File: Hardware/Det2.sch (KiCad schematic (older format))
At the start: 48 parts, among them U3 MAX4477, U4 MAX4477, U5 MAX4477

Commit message: Clear annotations
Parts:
- renumbered C22 to C?, C28 to C?, C30 to C?, C26 to C?, C27 to C?, C29 to C?, C31 to C?, C32 to C?, C23 to C?, C24 to C?, C35 to C?, C33 to C?, C34 to C?, C25 to C?, C7 to C?, C46 to C?, D34 to D?, D32 to D?, D30 to D?, D28 to D?, D26 to D?, D24 to D?, D22 to D?, D20 to D?, D35 to D?, D33 to D?, D31 to D?, D29 to D?, D27 to D?, D25 to D?, D23 to D?, D21 to D?, R22 to R?, R24 to R?, R28 to R?, R29 to R?, R30 to R?, R25 to R?, R31 to R?, R32 to R?, R26 to R?, R27 to R?, R23 to R?, R40 to R?, R20 to R?, U3 to U?, U4 to U?, U5 to U?

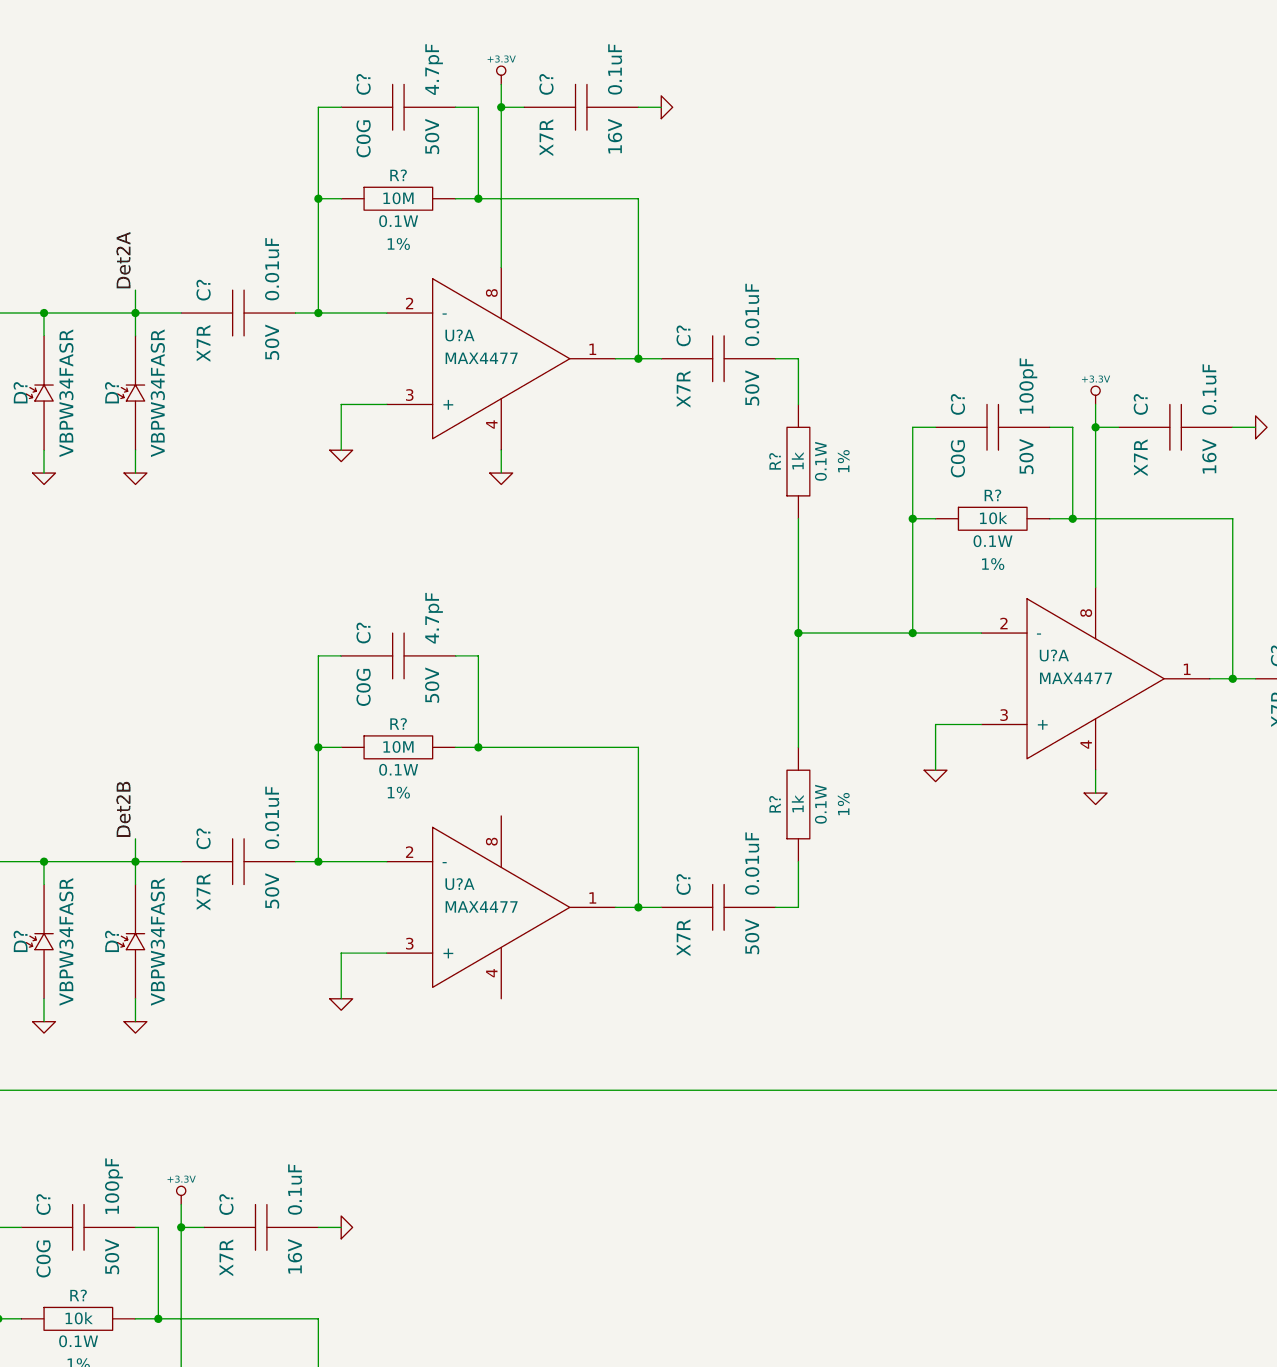
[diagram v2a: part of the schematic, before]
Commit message: Add LDO for analog
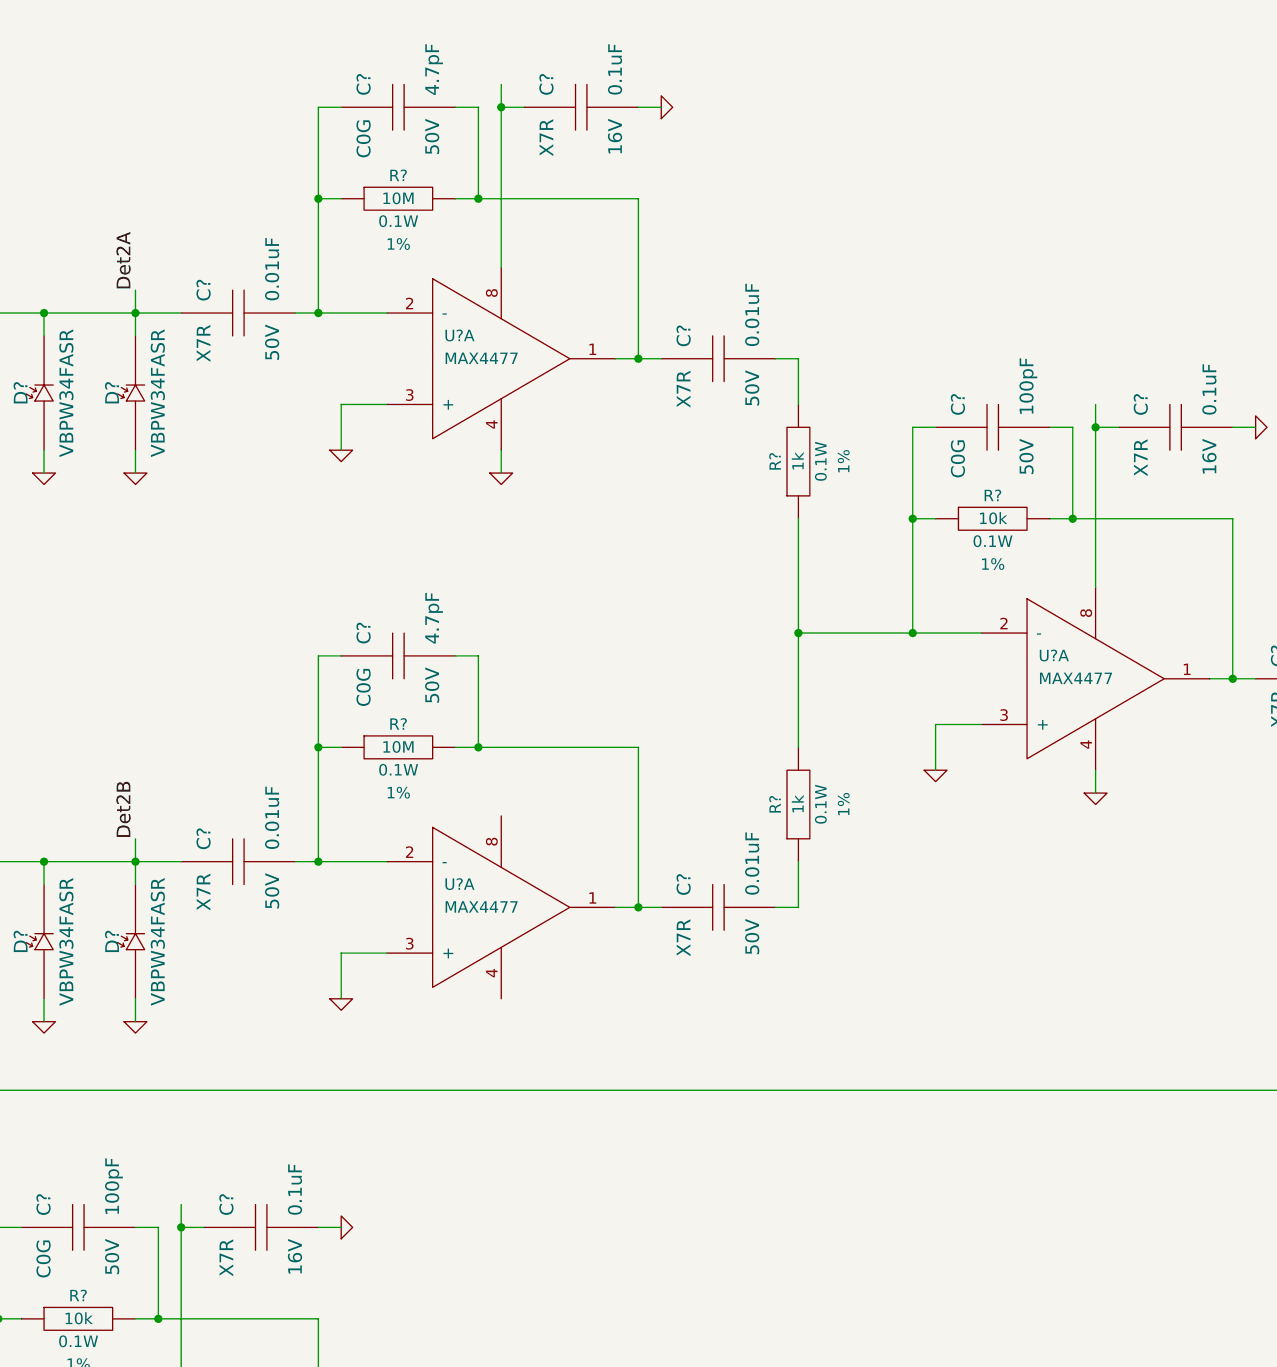
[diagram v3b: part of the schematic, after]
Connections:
- net labels removed: +3.3V
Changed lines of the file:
@@
 Sheet 4 5
 Title "Solid State Cosmic Ray Detector"
-Date "22 sep 2014"
+Date "23 sep 2014"
 Rev "1"
 Comp "Ethan Harstad"
@@
 $EndComp
 $Comp
-L +3.3V #PWR?
-U 1 1 52B9581C
-P 6200 900
-F 0 "#PWR?" H 6200 860 30  0001 C CNN
-F 1 "+3.3V" H 6200 1010 30  0000 C CNN
-F 2 "" H 6200 900 60  0000 C CNN
-F 3 "" H 6200 900 60  0000 C CNN
-	1    6200 900
-	1    0    0    -1
-$EndComp
-$Comp
 L C C?
 U 1 1 52B95827
@@
 	0    -1   -1   0
 $EndComp
-$Comp
-L +3.3V #PWR?
-U 1 1 52B95997
-P 8800 2300
-F 0 "#PWR?" H 8800 2260 30  0001 C CNN
-F 1 "+3.3V" H 8800 2410 30  0000 C CNN
-F 2 "" H 8800 2300 60  0000 C CNN
-F 3 "" H 8800 2300 60  0000 C CNN
-	1    8800 2300
-	1    0    0    -1
-$EndComp
 Wire Wire Line
 	7400 4500 7500 4500
@@
 $EndComp
 $Comp
-L +3.3V #PWR?
-U 1 1 52BB5C92
-P 4800 5800
-F 0 "#PWR?" H 4800 5760 30  0001 C CNN
-F 1 "+3.3V" H 4800 5910 30  0000 C CNN
-F 2 "" H 4800 5800 60  0000 C CNN
-F 3 "" H 4800 5800 60  0000 C CNN
-	1    4800 5800
-	1    0    0    -1
-$EndComp
-$Comp

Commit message: New detector chain
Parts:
- removed C? (x5): 0.1uF, CAPC1608, symbol C
- removed C? (x2): 4.7pF, CAPC1608, symbol C
- removed C? (x6): 0.01uF, CAPC1608, symbol C
- removed C? (x3): 100pF, CAPC1608, symbol C
- removed D? (x16): VBPW34FASR, DIOC-BPW34R, symbol DIODE-PHOTO
- removed R? (x2): 1M, RESC1608, symbol R
- removed R? (x4): 10M, RESC1608, symbol R
- removed R? (x4): 1k, RESC1608, symbol R
- removed R? (x3): 10k, RESC1608, symbol R
- removed U? (x5): MAX4477, symbol OPAMP-DUAL
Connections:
- net labels removed: +12V, Det2A, Det2B, GND, Out
- wire segments 120 -> 0

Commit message: Add second detector chain
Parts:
- added C? (x5): 0.1uF, CAPC1608, symbol C
- added C? (x5): 1000pF, CAPC1608, symbol C
- added C? (x2): C, ~, symbol C
- added D? (x16): VBPW34FASR, DIOC-BPW34R, symbol DIODE-PHOTO
- added R? (x4): 1M, RESC1608, symbol R
- added R? (x2): 10M, RESC1608, symbol R
- added R? (x3): 100k, ~, symbol R
- added R? (x4): 10k, RESC1608, symbol R
- added U? (x5): AD8616, ~, symbol OPAMP-DUAL
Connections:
- new net: C?.1, R?.1, R?.1 (x2)
- new net: C?.1, C?.2, R?.1, U?.2 (-) (x2)
- new net: C?.1, C?.2, R?.2, U?.1 (x2)
- new net: R?.1, R?.1, R?.2, U?.2 (-)
- new net: R?.2, R?.2, U?.1
- new net: C?.2, R?.2
- new net: C?.2, R?.1
- new net: C?.1, R?.1, R?.1, U?.2 (-)
- new net: C?.2, R?.2, R?.2, U?.1
- new net: R?.1, R?.1, U?.2 (-)
- new net Det1A: C?.1, D?.2, D?.2, D?.2, D?.2, D?.2, D?.2, D?.2, D?.2, R?.2
- new net Det1B: C?.1, D?.2, D?.2, D?.2, D?.2, D?.2, D?.2, D?.2, D?.2, R?.2
- new net GND: C?.2, C?.2, C?.2, C?.2, C?.2, D?.1, D?.1, D?.1, D?.1, D?.1, D?.1, D?.1, D?.1, D?.1, D?.1, D?.1, D?.1, D?.1, D?.1, D?.1, D?.1, U?.4, U?.4, U?.4
- new net Out: R?.2, U?.1
- new net Ref: U?.3 (+), U?.3 (+), U?.3 (+), U?.3 (+), U?.3 (+)
- new net VAA: C?.1, C?.1, C?.1, U?.8, U?.8, U?.8
- new net VCOM: R?.2, R?.2
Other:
- note added: "Charge Amplifier"
- note added: "Differentiator Amplifier"
- note added: "Final Amplifier"
- note added: "Integrator Amplifier"
- note added: "Light Shielding"
- note added: "Summing"

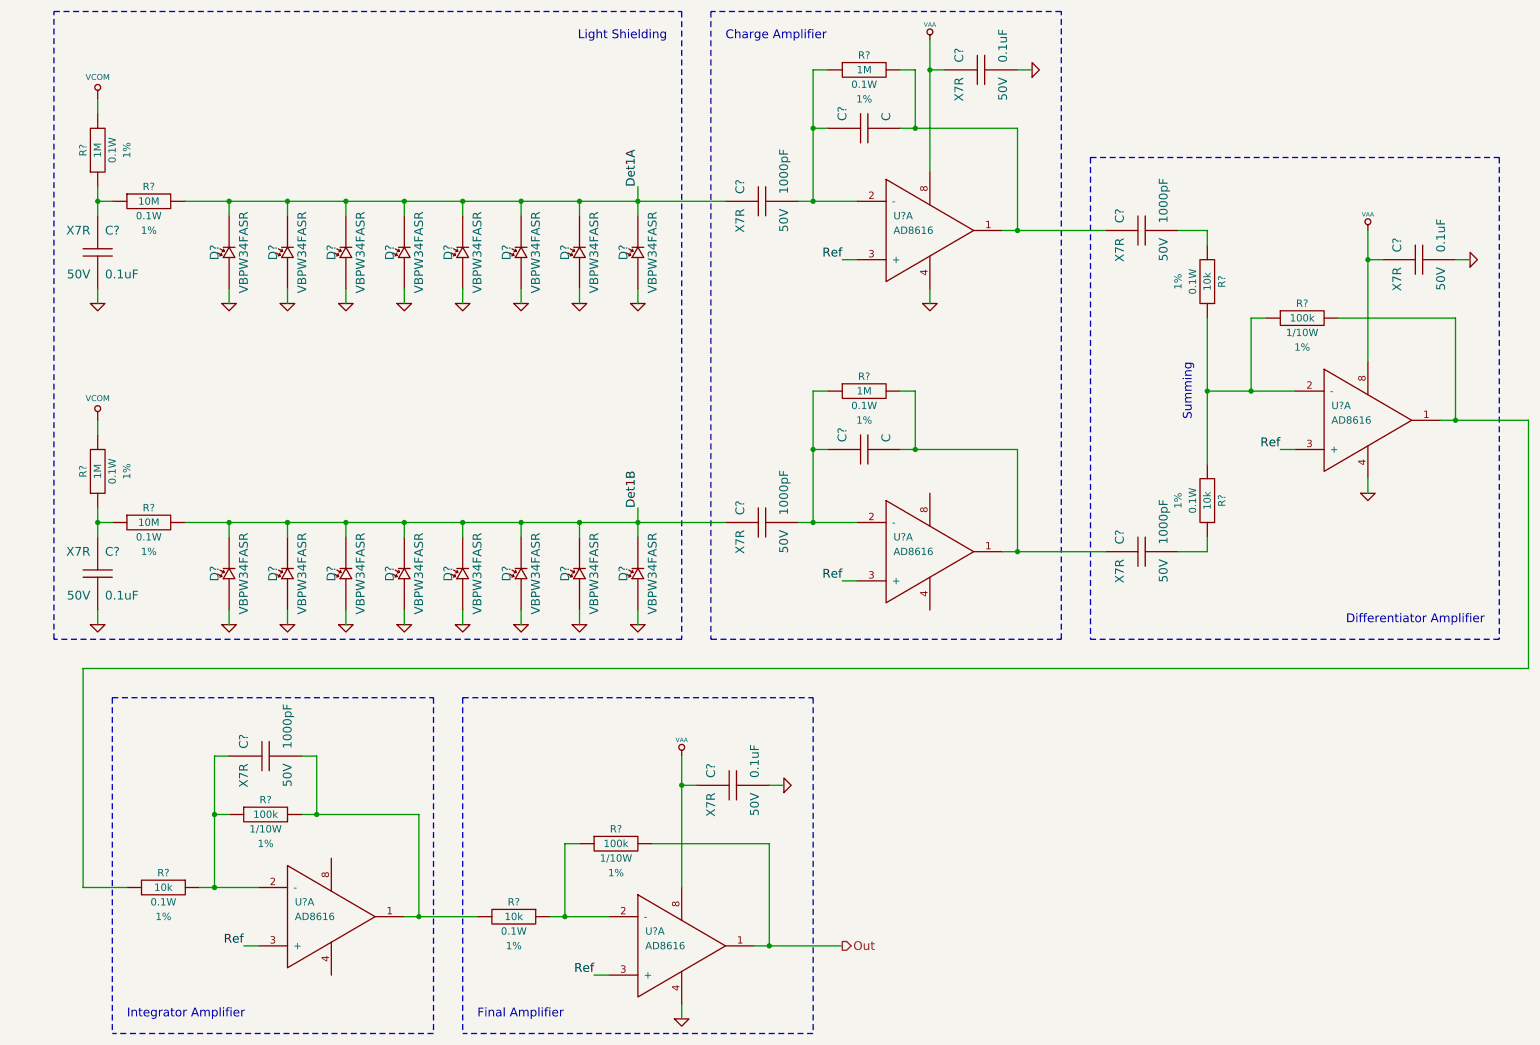
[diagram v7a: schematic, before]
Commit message: Rough layout for pin map testing
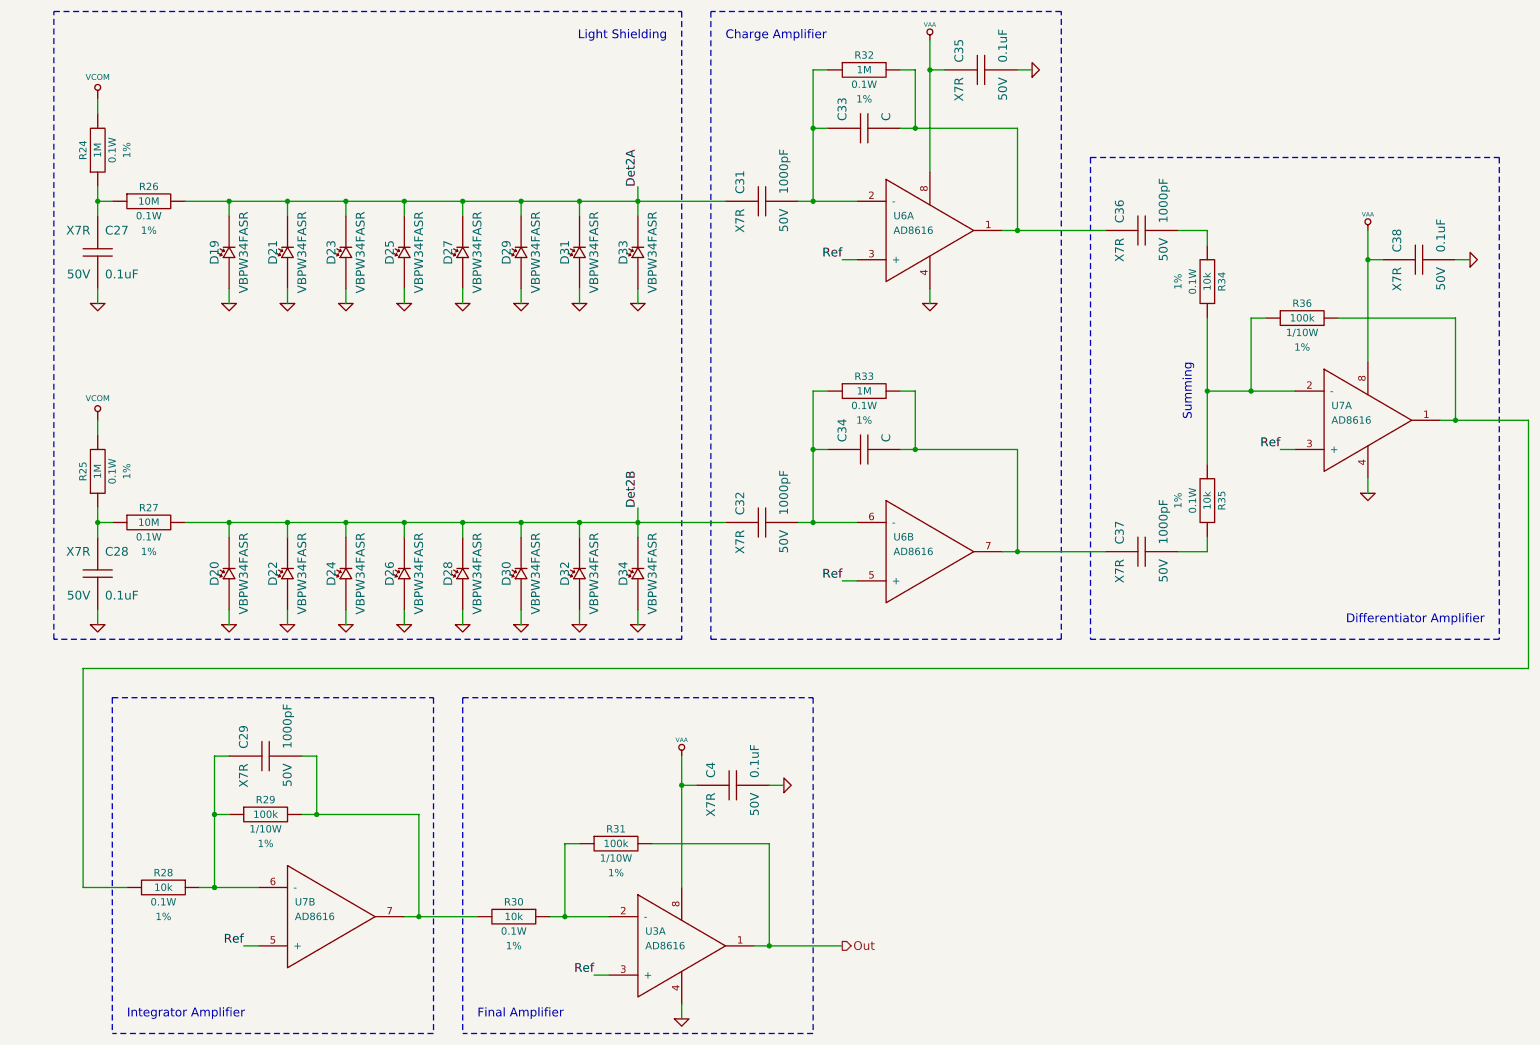
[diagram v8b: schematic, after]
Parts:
- removed C?: 0.1uF, CAPC1608, symbol C
- added C4: 0.1uF, CAPC1608, symbol C
- gave numbers to parts that had none: 43
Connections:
- net GND: now also U3.4, U7.4, C4.2; no longer U6.4, U7.4
- net Out: now also U3.1; no longer U6.1
- net Ref: now also U6.5 (+), U7.5 (+); no longer U6.3 (+), U7.3 (+)
- net VAA: now also U3.8, U7.8, C4.1; no longer U6.8, U7.8
- net at C31.2, C33.1, R32.1: now also U6.2 (-); no longer U6.2 (-)
- net at C33.2, C36.1, R32.2: now also U6.1; no longer U6.1
- net at C32.2, C34.1, R33.1: now also U6.6 (-); no longer U7.2 (-)
- net at C34.2, C37.1, R33.2: now also U6.7; no longer U7.1
- net at R34.1, R35.2, R36.1: now also U7.2 (-); no longer U7.2 (-)
- net at R28.2, R36.2: now also U7.1; no longer U7.1
- net at C29.1, R28.1, R29.1: now also U7.6 (-); no longer U3.2 (-)
- net at C29.2, R29.2, R30.2: now also U7.7; no longer U3.1
- net at R30.1, R31.1: now also U3.2 (-); no longer U6.2 (-)
- net Det1A renamed Det2A
- net Det1B renamed Det2B
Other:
- moved on the sheet: U3A, U6A, U7A
